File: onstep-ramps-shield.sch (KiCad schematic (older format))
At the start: 29 parts

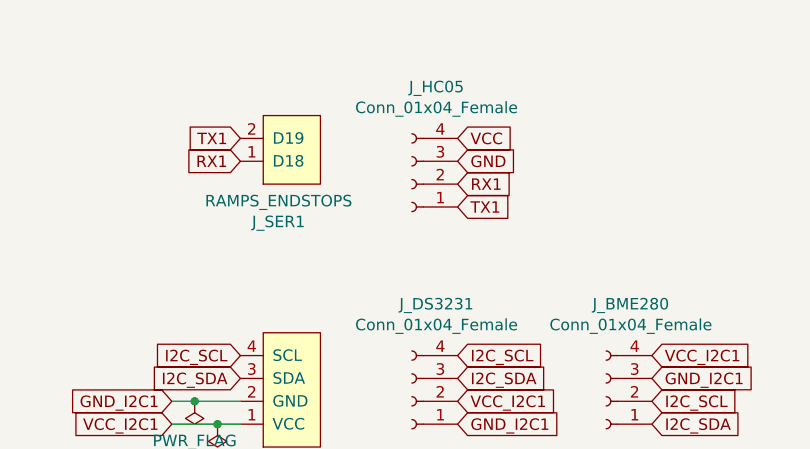
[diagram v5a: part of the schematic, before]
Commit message: Add voltage divider for HC05
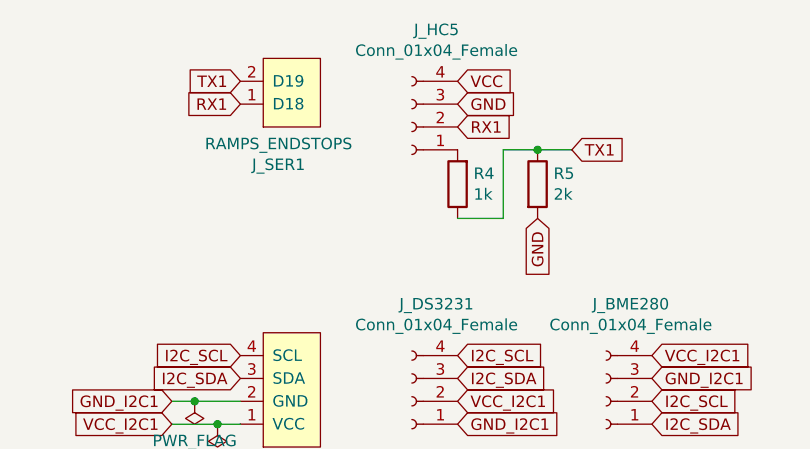
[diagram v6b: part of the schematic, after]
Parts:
- added R4: 1k, Resistor_SMD:R_0603_1608Metric_Pad1.05x0.95mm_HandSolder, symbol Device:R
- added R5: 2k, Resistor_SMD:R_0603_1608Metric_Pad1.05x0.95mm_HandSolder, symbol Device:R
- renumbered J_HC05 to J_HC5
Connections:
- net GND: now also R5.2
- net TX1: now also R4.1, R5.1; no longer J_HC5.1 (Pin_1)
- new net: J_HC5.1 (Pin_1), R4.2
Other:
- moved on the sheet: J_HC5, J_SER1
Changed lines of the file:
@@
 L OnstepRampsShield:RAMPS_ENDSTOPS J_SER1
 U 1 1 5F4D74CE
-P 5950 1450
-F 0 "J_SER1" V 5635 1433 50  0000 C CNN
-F 1 "RAMPS_ENDSTOPS" V 5726 1433 50  0000 C CNN
-F 2 "Connector_PinSocket_2.54mm:PinSocket_1x02_P2.54mm_Vertical" H 5950 1450 50  0001 C CNN
-F 3 "" H 5950 1450 50  0001 C CNN
-	1    5950 1450
+P 5950 1200
+F 0 "J_SER1" V 5635 1183 50  0000 C CNN
+F 1 "RAMPS_ENDSTOPS" V 5726 1183 50  0000 C CNN
+F 2 "Connector_PinSocket_2.54mm:PinSocket_1x02_P2.54mm_Vertical" H 5950 1200 50  0001 C CNN
+F 3 "" H 5950 1200 50  0001 C CNN
+	1    5950 1200
 	0    -1   -1   0
 $EndComp
@@
 Text GLabel 3250 3900 1    50   Input ~ 0
 STATUS_LED2
-Text GLabel 5800 1400 0    50   Input ~ 0
+Text GLabel 5800 1150 0    50   Input ~ 0
 TX1
-Text GLabel 5800 1500 0    50   Input ~ 0
+Text GLabel 5800 1250 0    50   Input ~ 0
 RX1
 NoConn ~ 3100 6200
@@
 $EndComp
 $Comp
-L Connector:Conn_01x04_Female J_HC05
+L Connector:Conn_01x04_Female J_HC5
 U 1 1 5F53C3AF
-P 6550 1600
-F 0 "J_HC05" H 6442 1175 50  0000 C CNN
-F 1 "Conn_01x04_Female" H 6442 1266 50  0000 C CNN
-F 2 "Connector_PinSocket_2.54mm:PinSocket_1x04_P2.54mm_Vertical" H 6550 1600 50  0001 C CNN
-F 3 "~" H 6550 1600 50  0001 C CNN
-	1    6550 1600
+P 6550 1350
+F 0 "J_HC5" H 6442 925 50  0000 C CNN
+F 1 "Conn_01x04_Female" H 6442 1016 50  0000 C CNN
+F 2 "Connector_PinSocket_2.54mm:PinSocket_1x04_P2.54mm_Vertical" H 6550 1350 50  0001 C CNN
+F 3 "~" H 6550 1350 50  0001 C CNN
+	1    6550 1350
 	-1   0    0    1
 $EndComp
@@
 Text GLabel 7600 2450 2    50   Input ~ 0
 GND_I2C1
-Text GLabel 6750 1400 2    50   Input ~ 0
+Text GLabel 6750 1150 2    50   Input ~ 0
 VCC
-Text GLabel 6750 1500 2    50   Input ~ 0
+Text GLabel 6750 1250 2    50   Input ~ 0
 GND
-Text GLabel 6750 1600 2    50   Input ~ 0
+Text GLabel 6750 1350 2    50   Input ~ 0
 RX1
-Text GLabel 6750 1700 2    50   Input ~ 0
+Text GLabel 7250 1450 2    50   Input ~ 0
 TX1
 NoConn ~ 5800 3100
@@
 NoConn ~ 3350 3900
 NoConn ~ 1850 3900
+$Comp
+L Device:R R4
+U 1 1 5F53F1FB
+P 6750 1600
+F 0 "R4" H 6680 1554 50  0000 R CNN
+F 1 "1k" H 6680 1645 50  0000 R CNN
+F 2 "Resistor_SMD:R_0603_1608Metric_Pad1.05x0.95mm_HandSolder" V 6680 1600 50  0001 C CNN
+F 3 "~" H 6750 1600 50  0001 C CNN
+	1    6750 1600
+	-1   0    0    1
+$EndComp
+$Comp
+L Device:R R5
+U 1 1 5F53F606
+P 7100 1600
+F 0 "R5" H 7170 1646 50  0000 L CNN
+F 1 "2k" H 7170 1555 50  0000 L CNN
+F 2 "Resistor_SMD:R_0603_1608Metric_Pad1.05x0.95mm_HandSolder" V 7030 1600 50  0001 C CNN
+F 3 "~" H 7100 1600 50  0001 C CNN
+	1    7100 1600
+	1    0    0    -1
+$EndComp
+Wire Wire Line
+	7250 1450 7100 1450
+Wire Wire Line
+	7100 1450 6950 1450
+Wire Wire Line
+	6950 1450 6950 1750
+Wire Wire Line
+	6950 1750 6750 1750
+Connection ~ 7100 1450
+Text GLabel 7100 1750 3    50   Input ~ 0
+GND
 $EndSCHEMATC

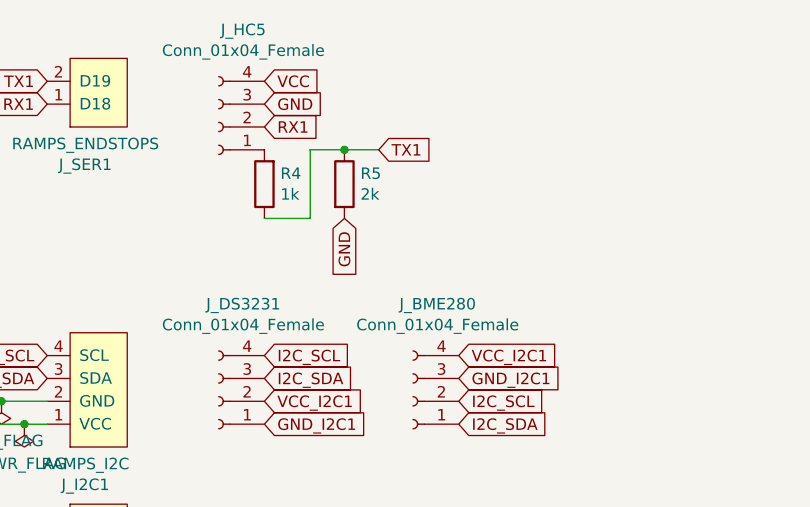
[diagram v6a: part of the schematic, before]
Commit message: Rearrange resistors
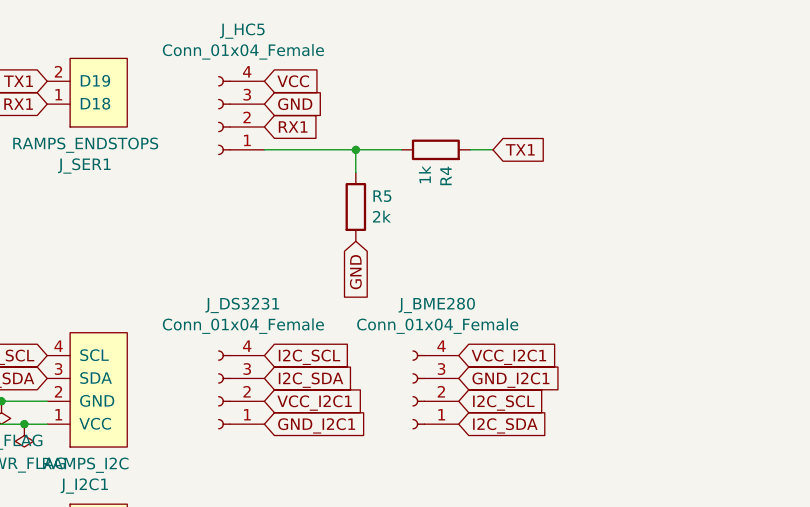
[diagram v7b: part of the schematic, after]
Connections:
- net TX1: now also R4.2; no longer R4.1, R5.1
- net at J_HC5.1 (Pin_1): now also R4.1, R5.1; no longer R4.2
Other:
- moved on the sheet: R4, R5
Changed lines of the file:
@@
 Text GLabel 6750 1350 2    50   Input ~ 0
 RX1
-Text GLabel 7250 1450 2    50   Input ~ 0
+Text GLabel 7750 1450 2    50   Input ~ 0
 TX1
 NoConn ~ 5800 3100
@@
 L Device:R R4
 U 1 1 5F53F1FB
-P 6750 1600
-F 0 "R4" H 6680 1554 50  0000 R CNN
-F 1 "1k" H 6680 1645 50  0000 R CNN
-F 2 "Resistor_SMD:R_0603_1608Metric_Pad1.05x0.95mm_HandSolder" V 6680 1600 50  0001 C CNN
-F 3 "~" H 6750 1600 50  0001 C CNN
-	1    6750 1600
-	-1   0    0    1
+P 7500 1450
+F 0 "R4" H 7430 1404 50  0000 R CNN
+F 1 "1k" H 7430 1495 50  0000 R CNN
+F 2 "Resistor_SMD:R_0603_1608Metric_Pad1.05x0.95mm_HandSolder" V 7430 1450 50  0001 C CNN
+F 3 "~" H 7500 1450 50  0001 C CNN
+	1    7500 1450
+	0    -1   -1   0
 $EndComp
 $Comp
 L Device:R R5
 U 1 1 5F53F606
-P 7100 1600
-F 0 "R5" H 7170 1646 50  0000 L CNN
-F 1 "2k" H 7170 1555 50  0000 L CNN
-F 2 "Resistor_SMD:R_0603_1608Metric_Pad1.05x0.95mm_HandSolder" V 7030 1600 50  0001 C CNN
-F 3 "~" H 7100 1600 50  0001 C CNN
-	1    7100 1600
-	1    0    0    -1
-$EndComp
-Wire Wire Line
-	7250 1450 7100 1450
-Wire Wire Line
-	7100 1450 6950 1450
-Wire Wire Line
-	6950 1450 6950 1750
-Wire Wire Line
-	6950 1750 6750 1750
-Connection ~ 7100 1450
-Text GLabel 7100 1750 3    50   Input ~ 0
+P 7150 1700
+F 0 "R5" H 7220 1746 50  0000 L CNN
+F 1 "2k" H 7220 1655 50  0000 L CNN
+F 2 "Resistor_SMD:R_0603_1608Metric_Pad1.05x0.95mm_HandSolder" V 7080 1700 50  0001 C CNN
+F 3 "~" H 7150 1700 50  0001 C CNN
+	1    7150 1700
+	1    0    0    -1
+$EndComp
+Text GLabel 7150 1850 3    50   Input ~ 0
 GND
+Wire Wire Line
+	7750 1450 7650 1450
+Wire Wire Line
+	7350 1450 7150 1450
+Wire Wire Line
+	7150 1450 7150 1550
+Wire Wire Line
+	7150 1450 6750 1450
+Connection ~ 7150 1450
 $EndSCHEMATC
